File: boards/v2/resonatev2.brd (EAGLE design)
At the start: 55.3 x 32.4 mm, 37 parts, among them U1 CC1101RTK, Y1 26 mHz

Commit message: making a new board
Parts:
- removed C1: 10uf, adafruit:C0603
- removed U$1: RFD22301, RFD22301-11.25.13:RFD21733
- moved JP2 21.6 mm to (55.1, 50.4)
- moved JP1 20.8 mm to (35.6, 62.9)
- moved C2 2.95 mm to (35.5, 45.9)
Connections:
- removed net N$4: U$1.P$10, U$1.P$9
- removed net N$5: U$1.P$1, U$1.P$2
- removed net N$6: C1.1, U$1.P$14
- removed net N$7: C1.2, JP2.DTR
- removed net N$8: JP2.RXI, U$1.P$17
- removed net N$9: JP2.TXO, U$1.P$16
- removed net P5: JP1.TXO, U$1.P$6
- new net N$2: JP1.TXO, U1.2
- net GND: no longer JP2.GND, U$1.P$12, U$1.P$18, U$1.P$19
- net N$32: now also JP1.VCC
- net P2: no longer JP1.GND, U$1.P$3
- net P3: no longer JP1.CTS, U$1.P$4, U1.2
- net P4: now also JP1.RXI; no longer JP1.VCC, U$1.P$5
- net P6: now also JP1.CTS; no longer JP1.RXI, U$1.P$7
- net VCC: now also JP1.GND; no longer JP2.VCC, U$1.P$13
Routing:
- net P3: track 60.0 -> 0.00 mm, vias 5 -> 0
- net P2: track 44.6 -> 0.00 mm, vias 2 -> 0
- net P4: track 46.1 -> 19.3 mm
- net P5: track 26.0 -> 0.00 mm, vias 1 -> 0
- net N$6: track 22.8 -> 0.00 mm, vias 2 -> 0
- net N$3: track 20.5 -> 0.00 mm
- net VCC: track 96.7 -> 76.5 mm, vias 6 -> 4
- net P6: track 47.2 -> 27.6 mm, vias 2 -> 1
- net N$32: track 0.00 -> 17.6 mm
- net GND: track 106.1 -> 94.6 mm, vias 7 -> 5
- net N$9: track 5.46 -> 0.00 mm
- net N$8: track 5.21 -> 0.00 mm
- net N$7: track 3.54 -> 0.00 mm
- net N$5: track 1.40 -> 0.00 mm
- net N$4: track 1.27 -> 0.00 mm
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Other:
- board text removed: "1"
- board text removed: "2"
- board text removed: "3"
- board text removed: "4"
- board text removed: "5"
- board text removed: "6"
- board text removed: "G"

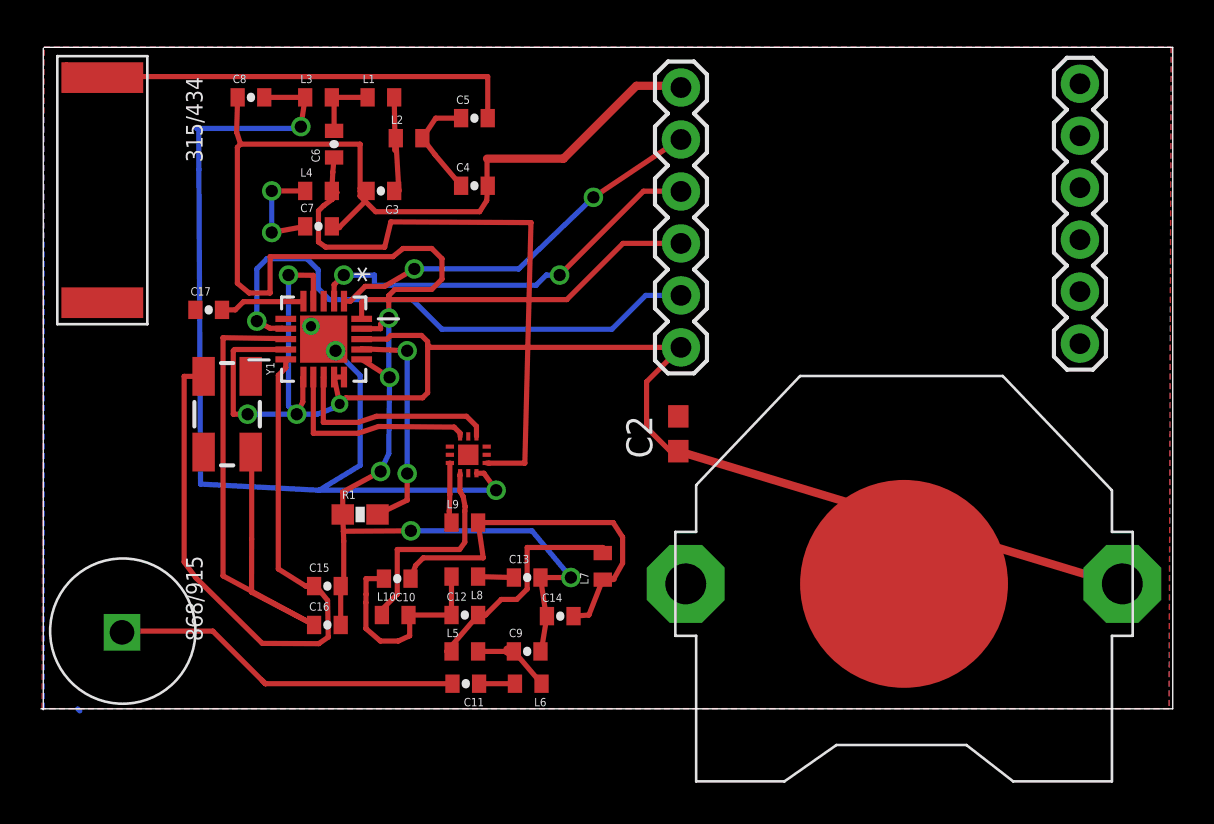
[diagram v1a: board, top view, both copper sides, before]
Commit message: adding new boards for nrf905
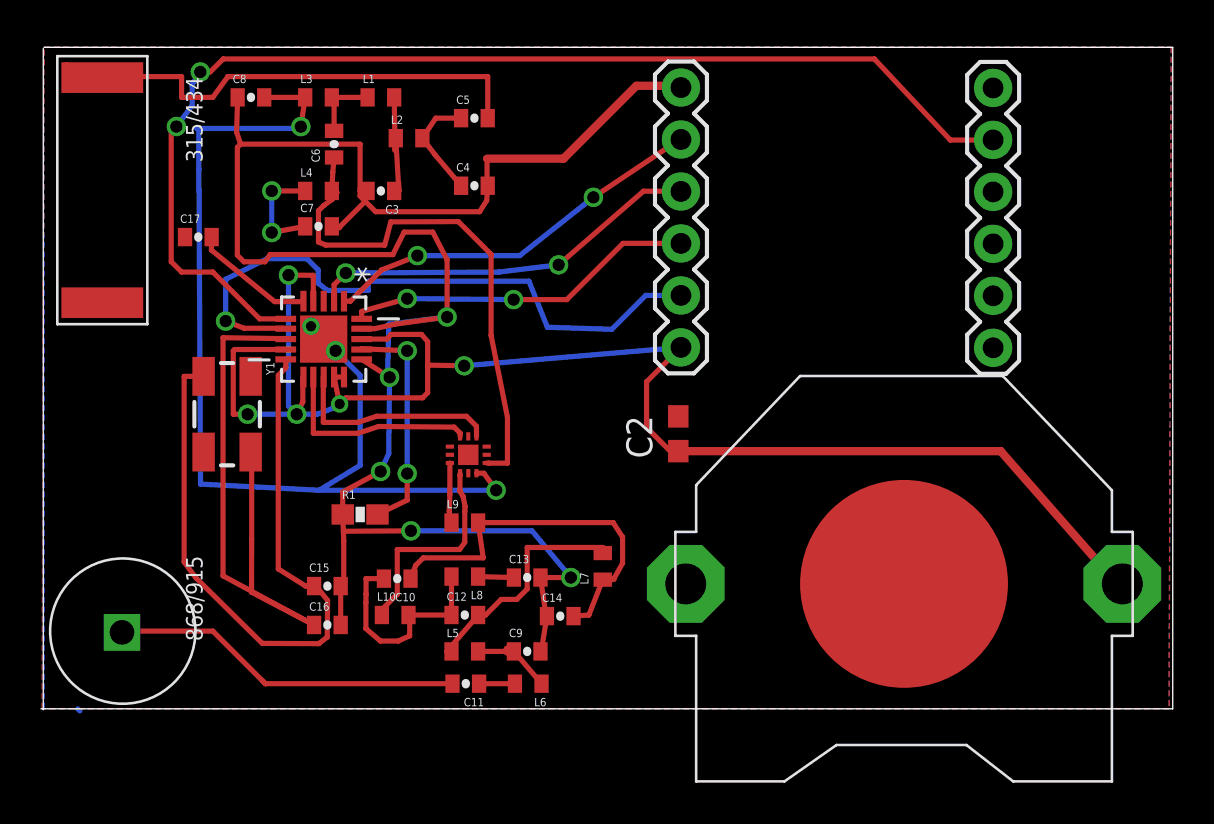
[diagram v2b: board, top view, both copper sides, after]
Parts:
- moved JP2 4.25 mm to (50.8, 50.1)
- moved C17 3.59 mm to (12.0, 55.6)
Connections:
- new net N$3: JP2.CTS, U1.6
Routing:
- net N$3: track 0.00 -> 57.2 mm, vias 0 -> 2
- net N$12: track 29.8 -> 26.0 mm
- net P6: track 27.6 -> 31.2 mm
- net VCC: track 76.5 -> 78.5 mm, vias 4 -> 5
- net N$34: track 4.24 -> 6.13 mm
- net N$22: track 20.7 -> 22.3 mm
- net GND: track 94.6 -> 96.0 mm
- net N$2: track 20.4 -> 19.4 mm
- net N$32: track 17.6 -> 17.2 mm, vias 0 -> 2
